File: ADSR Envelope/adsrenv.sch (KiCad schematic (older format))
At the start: 60 parts

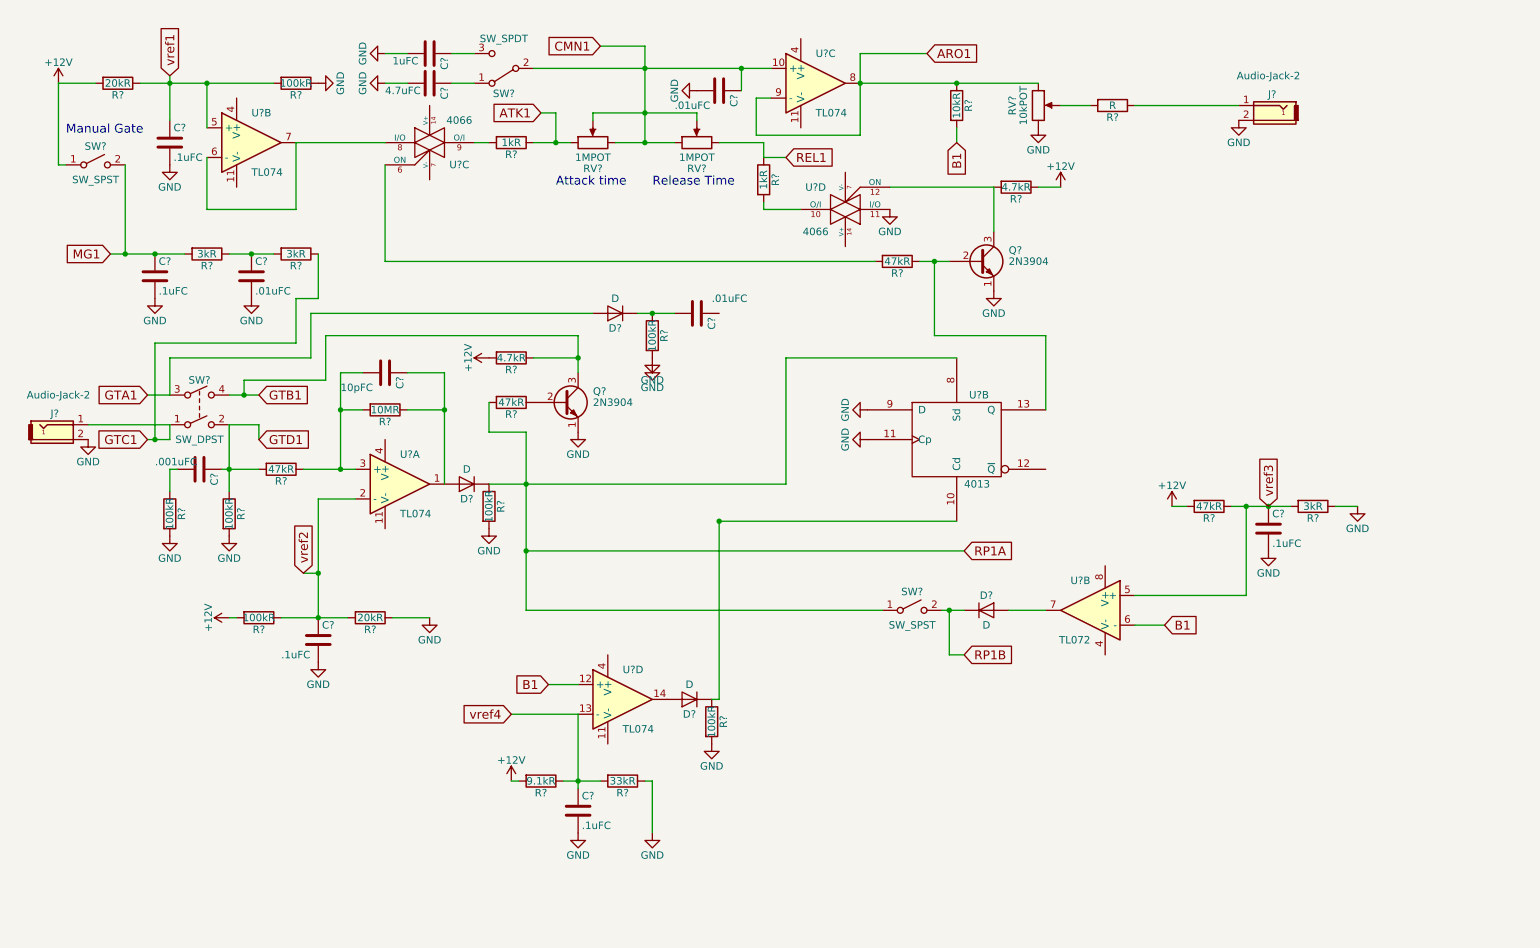
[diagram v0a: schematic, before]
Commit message: Schematic Capture of ADSR Env.
Missing EURORACK connector and SMD and THT layout
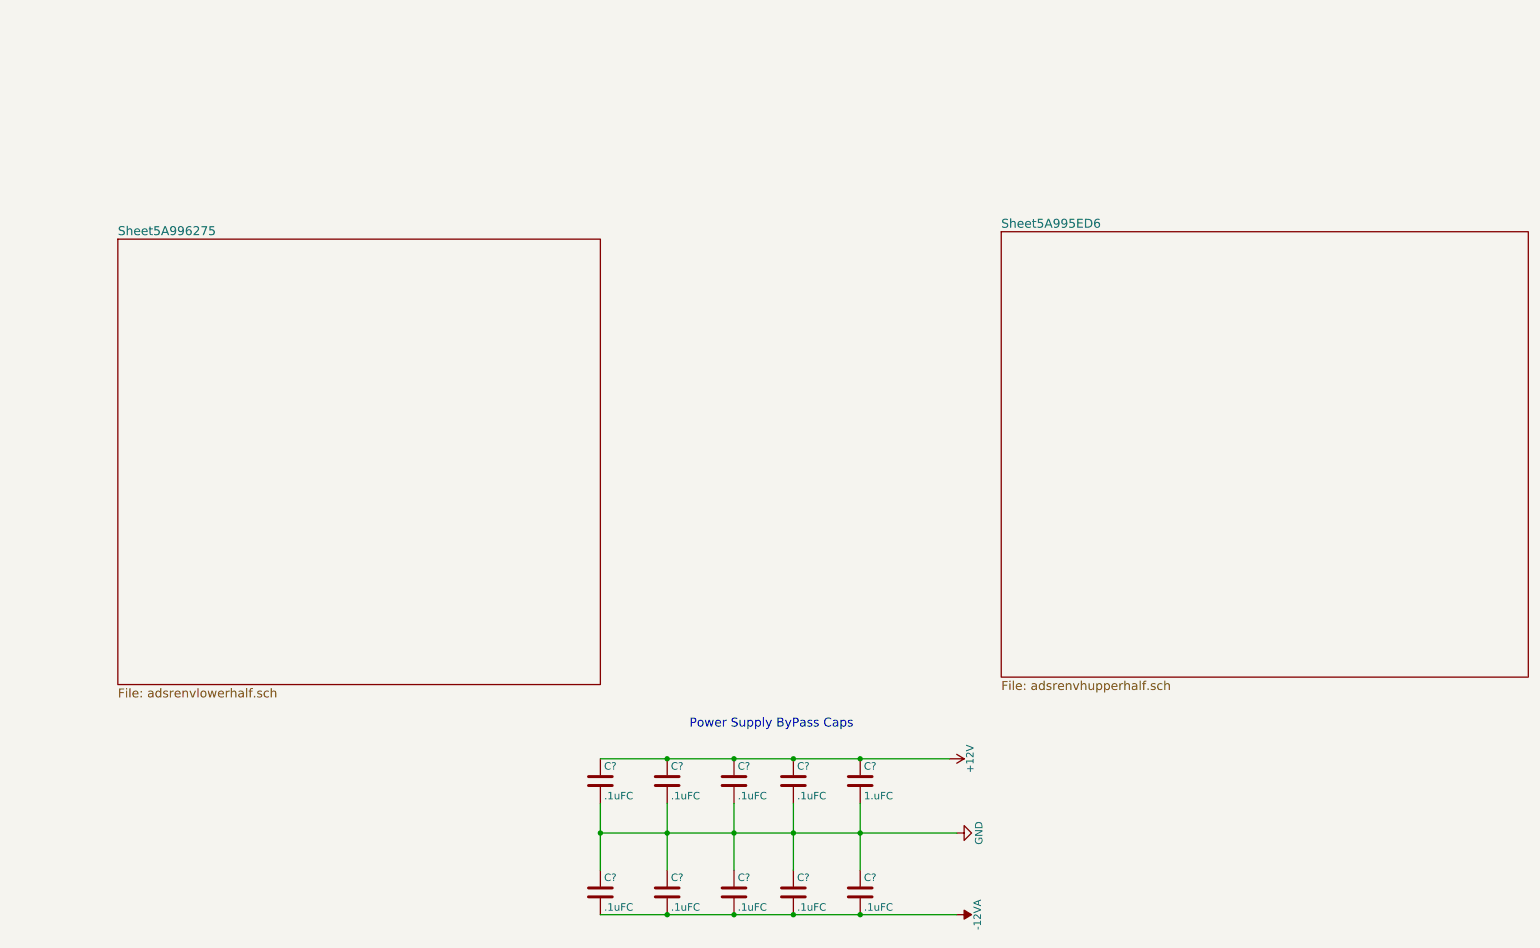
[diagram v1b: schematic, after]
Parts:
- removed C? (x5): .1uFC, symbol C
- removed C?: 1uFC, symbol C
- removed C?: 4.7uFC, symbol C
- removed C? (x3): .01uFC, symbol C
- removed C?: .001uFC, symbol C
- removed C?: 10pFC, symbol C
- removed D? (x4): D, symbol D
- removed J? (x2): Audio-Jack-2, symbol Audio-Jack-2
- removed Q? (x2): 2N3904, TO_SOT_Packages_THT:TO-92_Molded_Narrow, symbol 2N3904
- removed R? (x2): 20kR, symbol R
- removed R? (x7): 100kR, symbol R
- removed R? (x3): 3kR, symbol R
- removed R? (x2): 1kR, symbol R
- removed R?: 10kR, symbol R
- removed R?: R, symbol R
- removed R? (x4): 47kR, symbol R
- removed R? (x2): 4.7kR, symbol R
- removed R?: 10MR, symbol R
- removed R?: 9.1kR, symbol R
- removed R?: 33kR, symbol R
- removed RV? (x2): 1MPOT, symbol POT
- removed RV?: 10kPOT, symbol POT
- removed SW? (x2): SW_SPST, symbol SW_SPST
- removed SW?: SW_SPDT, symbol SW_SPDT
- removed SW?: SW_DPST, symbol SW_DPST
- removed U? (x4): TL074, symbol TL074
- removed U? (x2): 4066, symbol 4066
- removed U?: 4013, symbol 4013
- removed U?: TL072, symbol TL072
- added C? (x9): .1uFC, symbol C
- added C?: 1.uFC, symbol C
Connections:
- net +12V: now also C?.1, C?.1, C?.1, C?.1, C?.1
- net GND: now also C?.1, C?.1, C?.1, C?.1, C?.1, C?.2, C?.2, C?.2, C?.2, C?.2
- new net -12VA: C?.2, C?.2, C?.2, C?.2, C?.2
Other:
- note added: "Power Supply ByPass Caps\n"
- note removed: "Attack time\n"
- note removed: "Manual Gate\n"
- note removed: "Release Time"
